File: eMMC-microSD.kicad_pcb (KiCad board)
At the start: 4 copper layers, 92 x 35.5 mm, 145 parts, among them J1 Micro_SD_Card, J2 Micro_SD_Card, J3 Micro_SD_Card, J4 Micro_SD_Card, J5 Micro_SD_Card, U1 eMMC_5.1_BGA153, U2 eMMC_5.1_BGA153, U3 eMMC_5.1_BGA153, U4 eMMC_5.1_BGA153, U5 eMMC_5.1_BGA153

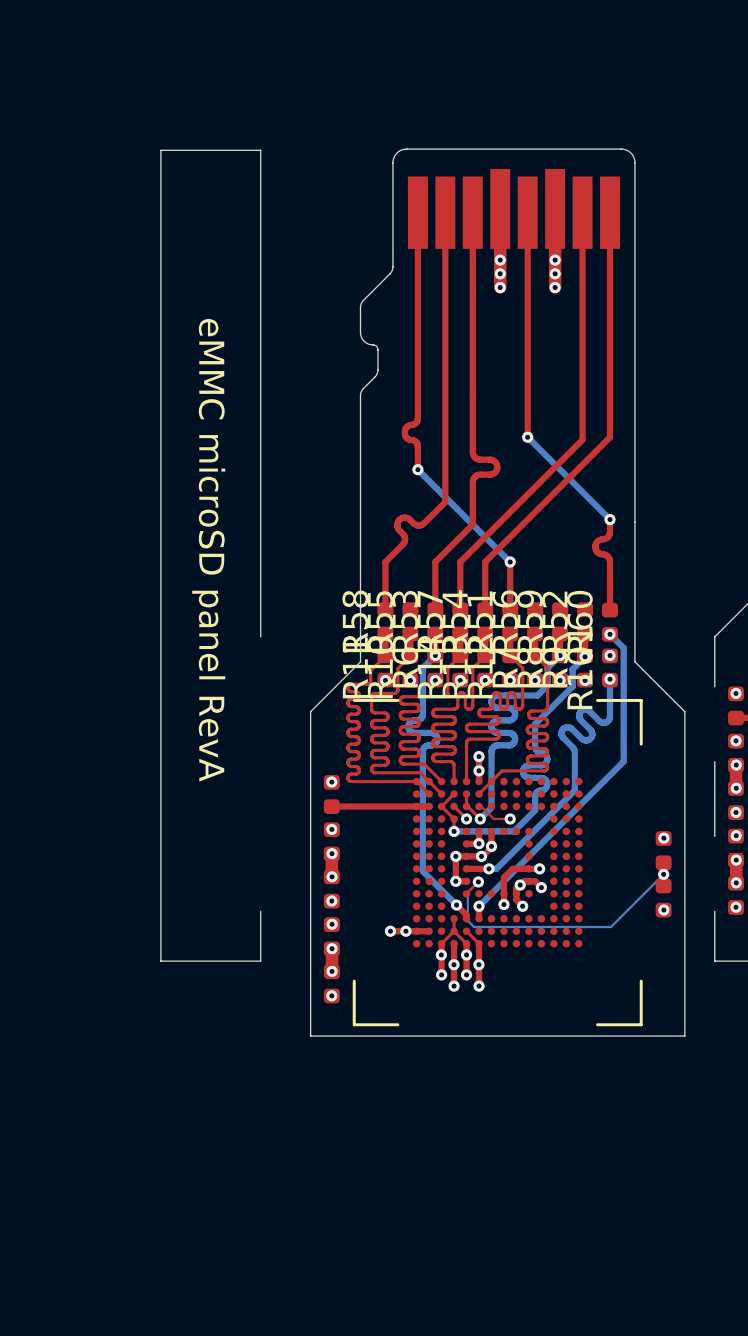
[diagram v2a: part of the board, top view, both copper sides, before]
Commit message: Fix incorrect D6 and D3 lengths
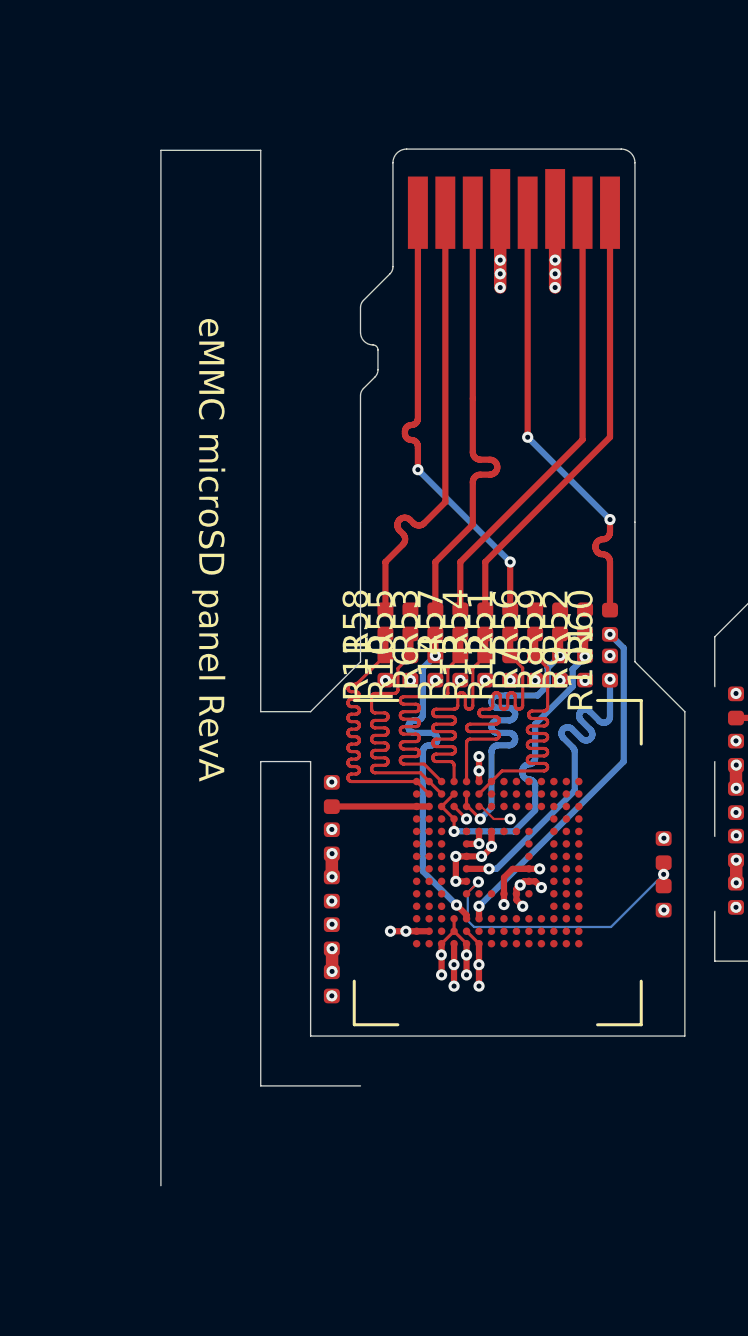
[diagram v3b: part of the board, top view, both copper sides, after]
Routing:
- net /Adapter 1/D5: track 15.5 -> 14.0 mm
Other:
- board size 92 x 35.5 mm -> 92 x 41.5 mm

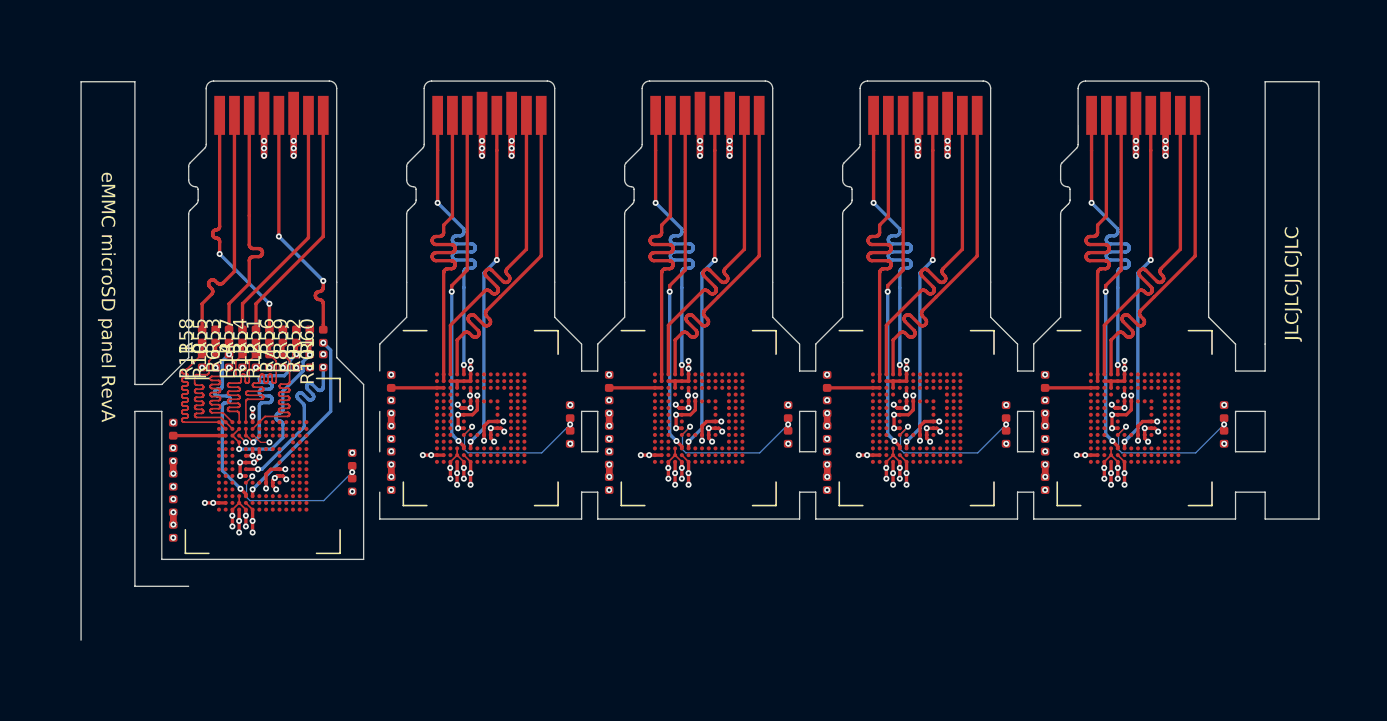
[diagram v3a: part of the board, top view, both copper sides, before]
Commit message: Finalize frame layout
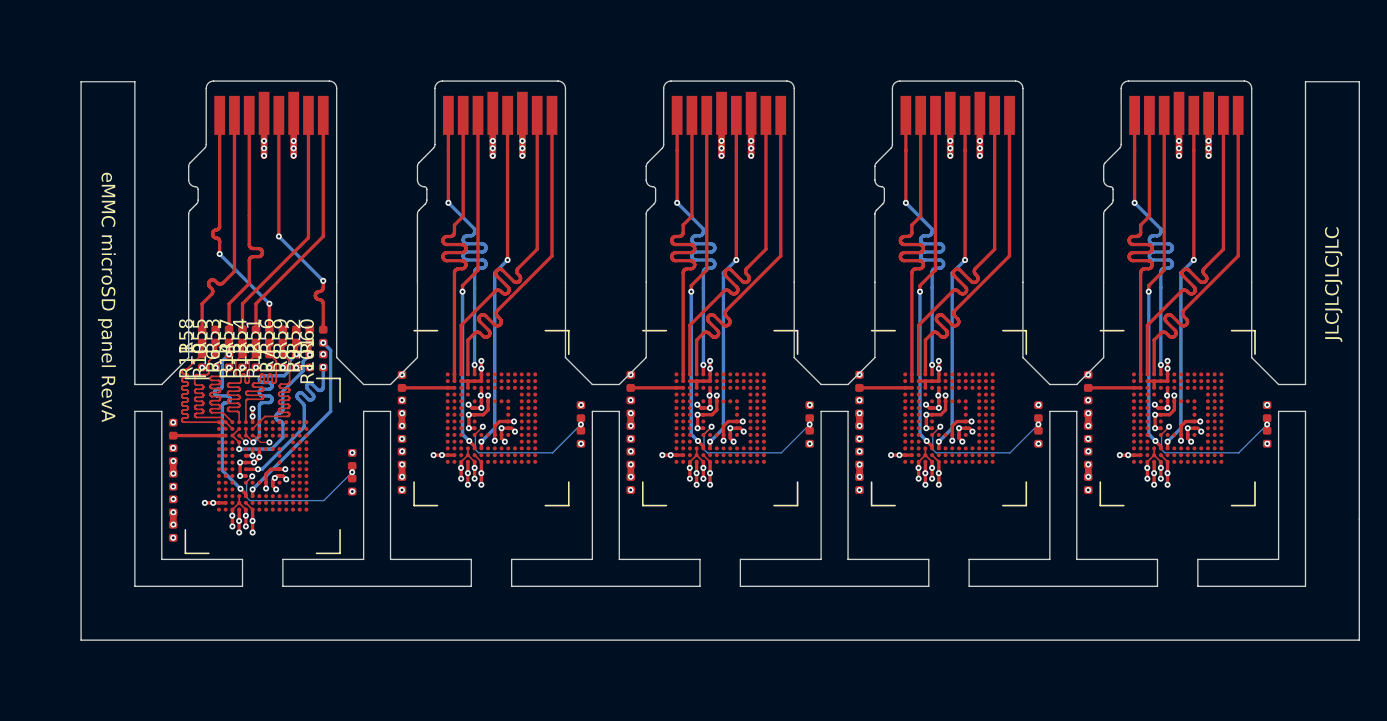
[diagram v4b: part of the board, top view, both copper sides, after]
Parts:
- moved C25 3.20 mm to (169.2, 137.0)
- moved J5 3.20 mm to (163.2, 115.0)
- moved R5 3.20 mm to (169.2, 138.9)
- moved C26 3.20 mm to (155.8, 134.8)
- moved C27 3.20 mm to (155.8, 140.5)
- moved C28 3.20 mm to (155.8, 138.6)
- moved C29 3.20 mm to (155.8, 142.4)
- moved C30 3.20 mm to (155.8, 136.7)
- moved U5 3.20 mm to (162.5, 137.5)
- moved C19 2.40 mm to (152.2, 137.0)
- moved C20 2.40 mm to (138.8, 134.8)
- moved C21 2.40 mm to (138.8, 140.5)
- moved C22 2.40 mm to (138.8, 138.6)
- moved C23 2.40 mm to (138.8, 142.4)
- moved C24 2.40 mm to (138.8, 136.7)
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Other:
- board size 92 x 41.5 mm -> 95 x 41.5 mm

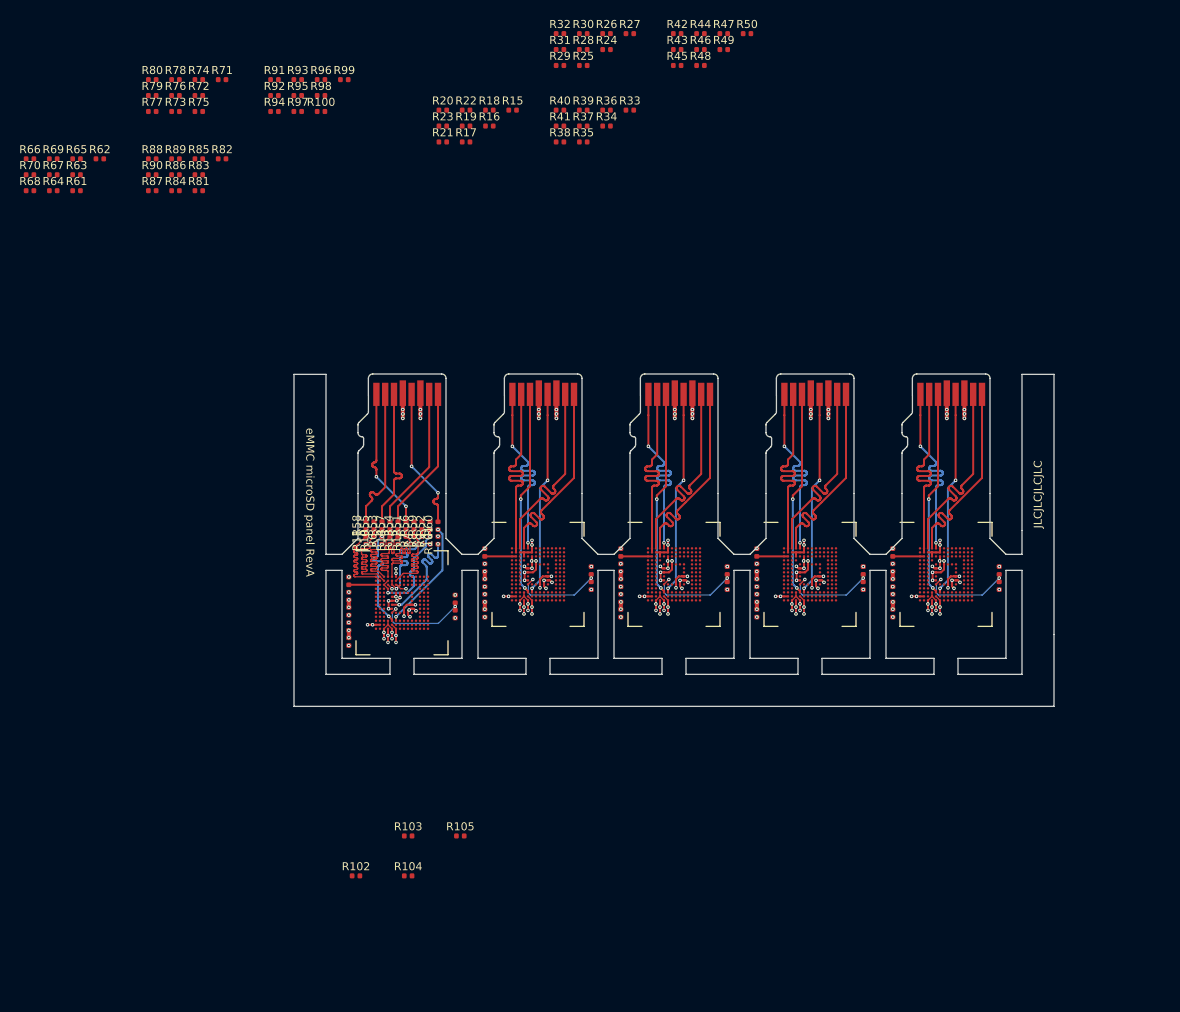
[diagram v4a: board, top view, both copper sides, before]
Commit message: Add mousebites to first adapter
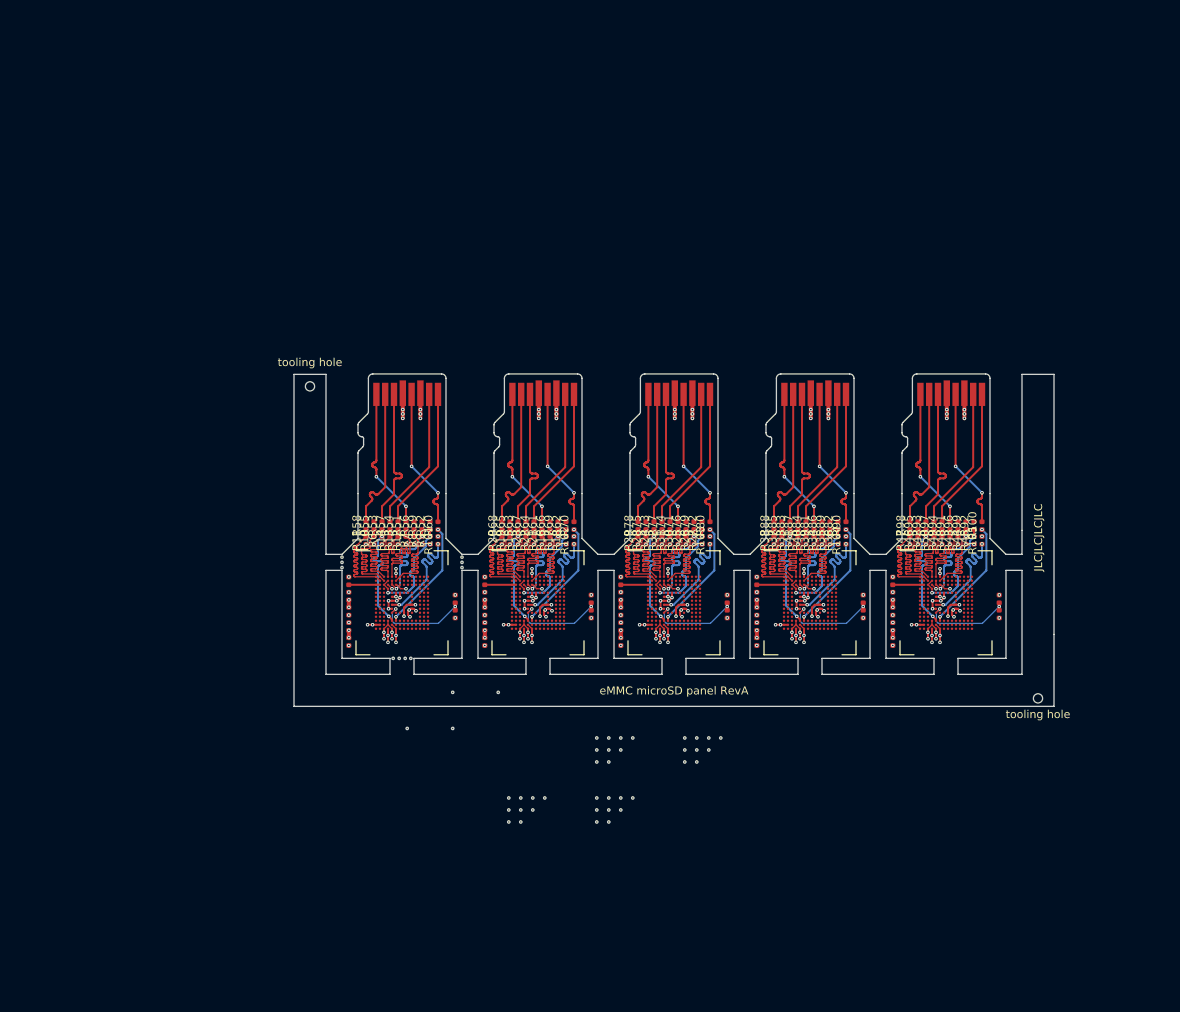
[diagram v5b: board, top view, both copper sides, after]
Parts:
- added H1: MountingHole, ToolingHole:ToolingHole_JLCSMT, F.Cu at (83.0, 114.0)
- added H10: MountingHole, Perforation:Perforation_0.3mm, F.Cu at (95.6, 148.0)
- added H11: MountingHole, Perforation:Perforation_0.3mm, F.Cu at (87.0, 136.0)
- added H12: MountingHole, Perforation:Perforation_0.3mm, F.Cu at (112.3, 165.4)
- added H13: MountingHole, Perforation:Perforation_0.3mm, F.Cu at (110.8, 166.9)
- added H14: MountingHole, Perforation:Perforation_0.3mm, F.Cu at (109.3, 168.4)
- added H15: MountingHole, Perforation:Perforation_0.3mm, F.Cu at (110.8, 165.4)
- added H16: MountingHole, Perforation:Perforation_0.3mm, F.Cu at (109.3, 166.9)
- added H17: MountingHole, Perforation:Perforation_0.3mm, F.Cu at (107.8, 165.4)
- added H18: MountingHole, Perforation:Perforation_0.3mm, F.Cu at (107.8, 168.4)
- added H19: MountingHole, Perforation:Perforation_0.3mm, F.Cu at (109.3, 165.4)
- added H2: MountingHole, ToolingHole:ToolingHole_JLCSMT, F.Cu at (174.0, 153.0)
- added H20: MountingHole, Perforation:Perforation_0.3mm, F.Cu at (107.8, 166.9)
- added H21: MountingHole, Perforation:Perforation_0.3mm, F.Cu at (121.8, 159.4)
- added H22: MountingHole, Perforation:Perforation_0.3mm, F.Cu at (120.3, 160.9)
- added H23: MountingHole, Perforation:Perforation_0.3mm, F.Cu at (121.8, 157.9)
- added H24: MountingHole, Perforation:Perforation_0.3mm, F.Cu at (123.3, 157.9)
- added H25: MountingHole, Perforation:Perforation_0.3mm, F.Cu at (120.3, 159.4)
- added H26: MountingHole, Perforation:Perforation_0.3mm, F.Cu at (118.8, 160.9)
- added H27: MountingHole, Perforation:Perforation_0.3mm, F.Cu at (120.3, 157.9)
- added H28: MountingHole, Perforation:Perforation_0.3mm, F.Cu at (118.8, 159.4)
- added H29: MountingHole, Perforation:Perforation_0.3mm, F.Cu at (118.8, 157.9)
- added H3: MountingHole, Perforation:Perforation_0.3mm, F.Cu at (93.4, 148.0)
- added H30: MountingHole, Perforation:Perforation_0.3mm, F.Cu at (123.3, 165.4)
- added H31: MountingHole, Perforation:Perforation_0.3mm, F.Cu at (121.8, 166.9)
- added H32: MountingHole, Perforation:Perforation_0.3mm, F.Cu at (120.3, 168.4)
- added H33: MountingHole, Perforation:Perforation_0.3mm, F.Cu at (121.8, 165.4)
- added H34: MountingHole, Perforation:Perforation_0.3mm, F.Cu at (120.3, 166.9)
- added H35: MountingHole, Perforation:Perforation_0.3mm, F.Cu at (118.8, 168.4)
- added H36: MountingHole, Perforation:Perforation_0.3mm, F.Cu at (120.3, 165.4)
- added H37: MountingHole, Perforation:Perforation_0.3mm, F.Cu at (118.8, 165.4)
- added H38: MountingHole, Perforation:Perforation_0.3mm, F.Cu at (118.8, 166.9)
- added H39: MountingHole, Perforation:Perforation_0.3mm, F.Cu at (129.8, 157.9)
- added H4: MountingHole, Perforation:Perforation_0.3mm, F.Cu at (87.0, 136.7)
- added H40: MountingHole, Perforation:Perforation_0.3mm, F.Cu at (129.8, 159.4)
- added H41: MountingHole, Perforation:Perforation_0.3mm, F.Cu at (131.3, 157.9)
- added H42: MountingHole, Perforation:Perforation_0.3mm, F.Cu at (129.8, 160.9)
- added H43: MountingHole, Perforation:Perforation_0.3mm, F.Cu at (131.3, 159.4)
- added H44: MountingHole, Perforation:Perforation_0.3mm, F.Cu at (132.8, 157.9)
- added H45: MountingHole, Perforation:Perforation_0.3mm, F.Cu at (131.3, 160.9)
- added H46: MountingHole, Perforation:Perforation_0.3mm, F.Cu at (132.8, 159.4)
- added H47: MountingHole, Perforation:Perforation_0.3mm, F.Cu at (134.3, 157.9)
- added H48: MountingHole, Perforation:Perforation_0.3mm, F.Cu at (94.9, 148.0)
- added H49: MountingHole, Perforation:Perforation_0.3mm, F.Cu at (95.2, 156.8)
- added H5: MountingHole, Perforation:Perforation_0.3mm, F.Cu at (102.0, 135.3)
- added H50: MountingHole, Perforation:Perforation_0.3mm, F.Cu at (100.8, 152.2)
- added H51: MountingHole, Perforation:Perforation_0.3mm, F.Cu at (100.8, 156.8)
- added H52: MountingHole, Perforation:Perforation_0.3mm, F.Cu at (106.5, 152.2)
- added H6: MountingHole, Perforation:Perforation_0.3mm, F.Cu at (94.2, 148.0)
- added H7: MountingHole, Perforation:Perforation_0.3mm, F.Cu at (87.0, 135.3)
- added H8: MountingHole, Perforation:Perforation_0.3mm, F.Cu at (102.0, 136.0)
- added H9: MountingHole, Perforation:Perforation_0.3mm, F.Cu at (102.0, 136.7)
- moved R92 102.6 mm to (166.0, 131.4), turned to 90 degrees
- moved R91 101.2 mm to (163.0, 131.4), turned to 90 degrees
- moved R94 98.2 mm to (162.0, 131.4), turned to 90 degrees
- moved R100 97.5 mm to (167.0, 131.4), turned to 90 degrees
- moved R96 97.2 mm to (164.0, 131.4), turned to 90 degrees
- moved R90 97.2 mm to (150.0, 131.4), turned to 90 degrees
- moved R93 96.3 mm to (160.0, 131.4), turned to 90 degrees
- moved R99 95.6 mm to (165.0, 131.4), turned to 90 degrees
- moved R97 94.9 mm to (161.0, 131.4), turned to 90 degrees
- moved R95 94.3 mm to (159.0, 131.4), turned to 90 degrees
- moved R89 93.8 mm to (148.0, 131.4), turned to 90 degrees
- moved R86 91.9 mm to (147.0, 131.4), turned to 90 degrees
- moved R98 91.2 mm to (158.0, 131.4), turned to 90 degrees
- moved R87 90.9 mm to (144.0, 131.4), turned to 90 degrees
- moved R88 90.2 mm to (141.0, 131.4), turned to 90 degrees
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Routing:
- net /Adapter 3/D3: track 0.00 -> 14.3 mm
- net /Adapter 2/D3: track 0.00 -> 14.3 mm
- net /Adapter 5/D3: track 0.00 -> 14.3 mm
- net /Adapter 4/D3: track 0.00 -> 14.3 mm
- net Net-(R50-Pad2): track 0.00 -> 14.1 mm
- net Net-(R41-Pad2): track 0.00 -> 14.1 mm
- net Net-(R32-Pad2): track 0.00 -> 14.1 mm
- net Net-(R23-Pad2): track 0.00 -> 14.1 mm
- net /Adapter 5/D6: track 0.00 -> 14.1 mm, vias 0 -> 2
- net /Adapter 4/D6: track 0.00 -> 14.1 mm, vias 0 -> 2
- net /Adapter 3/D6: track 0.00 -> 14.1 mm, vias 0 -> 2
- net /Adapter 2/D6: track 0.00 -> 14.1 mm, vias 0 -> 2
- net Net-(R31-Pad2): track 0.00 -> 14.1 mm
- net Net-(R22-Pad2): track 0.00 -> 14.1 mm
- net Net-(R49-Pad2): track 0.00 -> 14.1 mm
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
